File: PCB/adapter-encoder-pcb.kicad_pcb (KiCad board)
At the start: 4 copper layers, 14 x 15.6 mm, 33 parts, among them IC1 THVD2410VDRCR, M1 THRU_HOLE_PAD, M2 THRU_HOLE_PAD, U1 TLE5009E1000FUMA1, U2 STM32G031G6U6, U3 DF52-4S-0.8H(21), U4 SPX3819M5-L-3-3, U5 C2901617, U6 DF52-4S-0.8H(21), U7 SPX3819M5-L-3-3

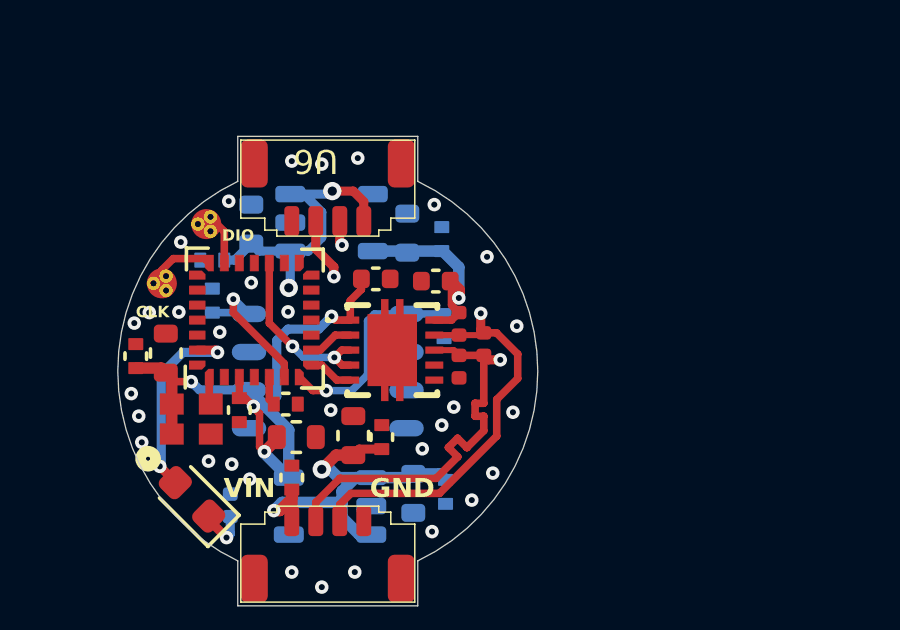
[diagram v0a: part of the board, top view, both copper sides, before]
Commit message: removed bad biasing resistors
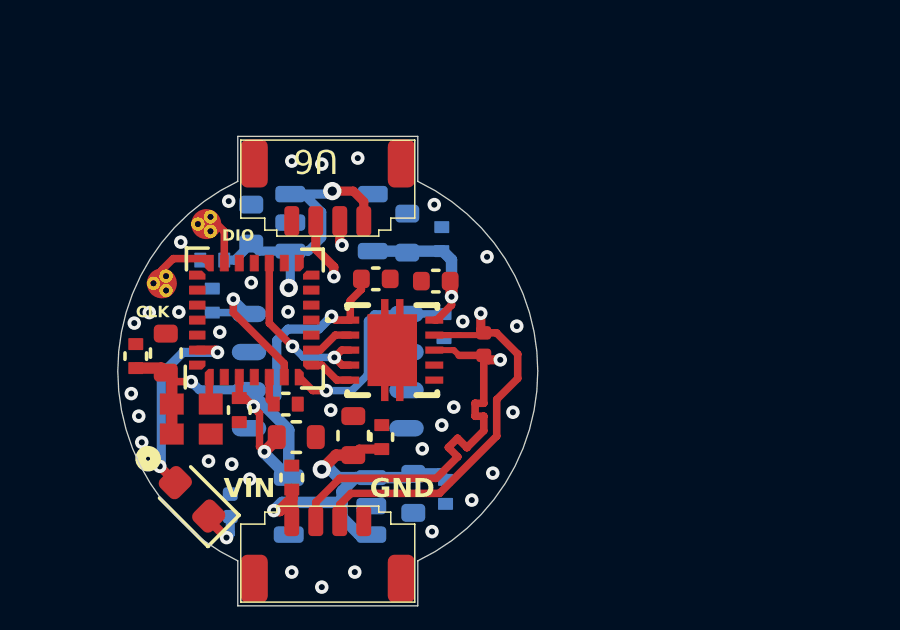
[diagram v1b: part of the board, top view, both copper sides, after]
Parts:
- removed R2, R4: 1k, adapter-encoder:R_0402_1005Metric
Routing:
- net /+5V0: track 6.90 -> 6.05 mm
- net GND: vias 31 -> 32
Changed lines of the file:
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@@
       (net 19 "/SWDIO") (pinfunction "1") (pintype "passive") (solder_mask_margin 0.0508))
-  )
-  (footprint "adapter-encoder:R_0402_1005Metric" (layer "F.Cu")
-    (at 149.279448 111.487448 90)
-    (descr "Resistor SMD 0402 (1005 Metric), square (rectangular) end terminal, IPC_7351 nominal, (Body size source: IPC-SM-782 page 72, https://www.pcb-3d.com/wordpress/wp-content/uploads/ipc-sm-782a_amendment_1_and_2.pdf), generated with kicad-footprint-generator")
-    (tags "resistor")
-    (property "Sheetfile" "adapter-encoder-pcb.kicad_sch")
-    (property "Sheetname" "")
-    (property "ki_description" "Resistor, US symbol")
-    (property "ki_keywords" "R res resistor")
-    (attr smd)
-    (fp_text reference "R4" (at 2.95 -1.45 90) (layer "F.SilkS") hide
-        (effects (font (size 1 1) (thickness 0.15)))
-    )
-    (fp_text value "1k" (at 0 1.17 90) (layer "F.Fab") hide
-        (effects (font (size 1 1) (thickness 0.15)))
-    )
-    (fp_text user "${REFERENCE}" (at 0 0 90) (layer "F.Fab")
-        (effects (font (size 0.26 0.26) (thickness 0.04)))
-    )
-    (fp_line (start -0.525 -0.27) (end 0.525 -0.27)
-      (stroke (width 0.1) (type solid)) (layer "F.Fab"))
-    (fp_line (start -0.525 0.27) (end -0.525 -0.27)
-      (stroke (width 0.1) (type solid)) (layer "F.Fab"))
-    (fp_line (start 0.525 -0.27) (end 0.525 0.27)
-      (stroke (width 0.1) (type solid)) (layer "F.Fab"))
-    (fp_line (start 0.525 0.27) (end -0.525 0.27)
-      (stroke (width 0.1) (type solid)) (layer "F.Fab"))
-    (pad "1" smd roundrect (at -0.375 0 90) (size 0.45 0.5) (layers "F.Cu" "F.Paste" "F.Mask") (roundrect_rratio 0.25)
-      (net 1 "GND") (pintype "passive") (solder_mask_margin 0.0508))
-    (pad "2" smd roundrect (at 0.375 0 90) (size 0.45 0.5) (layers "F.Cu" "F.Paste" "F.Mask") (roundrect_rratio 0.25)
-      (net 37 "/RS485+") (pintype "passive") (solder_mask_margin 0.0508))
-    (model "${KICAD6_3DMODEL_DIR}/Resistor_SMD.3dshapes/R_0402_1005Metric.wrl"
-      (offset (xyz 0 0 0))
-      (scale (xyz 1 1 1))
-      (rotate (xyz 0 0 0))
-    )
   )
   (footprint "adapter-encoder:C_0402_1005Metric" (layer "F.Cu")
@@
   )
   (footprint "adapter-encoder:R_0402_1005Metric" (layer "F.Cu")
-    (at 149.279448 110.062448 90)
-    (descr "Resistor SMD 0402 (1005 Metric), square (rectangular) end terminal, IPC_7351 nominal, (Body size source: IPC-SM-782 page 72, https://www.pcb-3d.com/wordpress/wp-content/uploads/ipc-sm-782a_amendment_1_and_2.pdf), generated with kicad-footprint-generator")
-    (tags "resistor")
-    (property "Sheetfile" "adapter-encoder-pcb.kicad_sch")
-    (property "Sheetname" "")
-    (property "ki_description" "Resistor, US symbol")
-    (property "ki_keywords" "R res resistor")
-    (attr smd)
-    (fp_text reference "R2" (at 2.95 -1.45 90) (layer "F.SilkS") hide
-        (effects (font (size 1 1) (thickness 0.15)))
-    )
-    (fp_text value "1k" (at 0 1.17 90) (layer "F.Fab") hide
-        (effects (font (size 1 1) (thickness 0.15)))
-    )
-    (fp_text user "${REFERENCE}" (at 0 0 90) (layer "F.Fab")
-        (effects (font (size 0.26 0.26) (thickness 0.04)))
-    )
-    (fp_line (start -0.525 -0.27) (end 0.525 -0.27)
-      (stroke (width 0.1) (type solid)) (layer "F.Fab"))
-    (fp_line (start -0.525 0.27) (end -0.525 -0.27)
-      (stroke (width 0.1) (type solid)) (layer "F.Fab"))
-    (fp_line (start 0.525 -0.27) (end 0.525 0.27)
-      (stroke (width 0.1) (type solid)) (layer "F.Fab"))
-    (fp_line (start 0.525 0.27) (end -0.525 0.27)
-      (stroke (width 0.1) (type solid)) (layer "F.Fab"))
-    (pad "1" smd roundrect (at -0.375 0 90) (size 0.45 0.5) (layers "F.Cu" "F.Paste" "F.Mask") (roundrect_rratio 0.25)
-      (net 38 "/RS485-") (pintype "passive") (solder_mask_margin 0.0508))
-    (pad "2" smd roundrect (at 0.375 0 90) (size 0.45 0.5) (layers "F.Cu" "F.Paste" "F.Mask") (roundrect_rratio 0.25)
-      (net 21 "/+5V0") (pintype "passive") (solder_mask_margin 0.0508))
-    (model "${KICAD6_3DMODEL_DIR}/Resistor_SMD.3dshapes/R_0402_1005Metric.wrl"
-      (offset (xyz 0 0 0))
-      (scale (xyz 1 1 1))
-      (rotate (xyz 0 0 0))
-    )
-  )
-  (footprint "adapter-encoder:R_0402_1005Metric" (layer "F.Cu")
     (at 150.104448 110.737448 90)
     (descr "Resistor SMD 0402 (1005 Metric), square (rectangular) end terminal, IPC_7351 nominal, (Body size source: IPC-SM-782 page 72, https://www.pcb-3d.com/wordpress/wp-content/uploads/ipc-sm-782a_amendment_1_and_2.pdf), generated with kicad-footprint-generator")
@@
   (via (at 148.054048 114.228248) (size 0.45) (drill 0.2) (layers "F.Cu" "B.Cu") (net 1))
   (via (at 145.004448 112.937448) (size 0.45) (drill 0.2) (layers "F.Cu" "B.Cu") (net 1))
+  (via (at 149.404448 109.983848) (size 0.45) (drill 0.2) (layers "F.Cu" "B.Cu") (net 1))
   (via (at 143.704448 118.337448) (size 0.45) (drill 0.2) (layers "F.Cu" "B.Cu") (net 1))
   (via (at 138.704448 114.012448) (size 0.45) (drill 0.2) (layers "F.Cu" "B.Cu") (net 1))
@@
   (segment (start 141.454448 106.982281) (end 140.984448 106.512281) (width 0.254) (layer "F.Cu") (net 20))
   (segment (start 141.454448 108.037448) (end 141.454448 106.982281) (width 0.254) (layer "F.Cu") (net 20))
-  (segment (start 149.273248 108.926248) (end 148.984448 108.637448) (width 0.4) (layer "F.Cu") (net 21))
-  (segment (start 149.029448 109.937448) (end 149.279448 109.687448) (width 0.254) (layer "F.Cu") (net 21))
   (segment (start 149.029448 108.682448) (end 149.029448 109.437448) (width 0.254) (layer "F.Cu") (net 21))
-  (segment (start 149.273248 109.199048) (end 149.273248 108.926248) (width 0.4) (layer "F.Cu") (net 21))
-  (segment (start 148.454448 109.937448) (end 149.029448 109.937448) (width 0.254) (layer "F.Cu") (net 21))
+  (segment (start 149.029448 109.157448) (end 149.029448 108.682448) (width 0.4) (layer "F.Cu") (net 21))
   (segment (start 148.984448 108.637448) (end 149.029448 108.682448) (width 0.254) (layer "F.Cu") (net 21))
-  (segment (start 149.029448 109.437448) (end 149.279448 109.687448) (width 0.254) (layer "F.Cu") (net 21))
-  (via (at 149.273248 109.199048) (size 0.45) (drill 0.2) (layers "F.Cu" "B.Cu") (net 21))
+  (segment (start 148.454448 109.937448) (end 148.529448 109.937448) (width 0.254) (layer "F.Cu") (net 21))
+  (segment (start 148.529448 109.937448) (end 149.029448 109.437448) (width 0.254) (layer "F.Cu") (net 21))
+  (via (at 149.029448 109.157448) (size 0.45) (drill 0.2) (layers "F.Cu" "B.Cu") (net 21))
+  (segment (start 149.029448 109.157448) (end 149.029448 107.927386) (width 0.381) (layer "B.Cu") (net 21))
+  (segment (start 149.029448 107.927386) (end 148.73951 107.637448) (width 0.381) (layer "B.Cu") (net 21))
+  (segment (start 148.704448 107.637448) (end 146.404448 107.637448) (width 0.381) (layer "B.Cu") (net 21))
   (segment (start 148.73951 107.637448) (end 148.704448 107.637448) (width 0.381) (layer "B.Cu") (net 21))
-  (segment (start 149.273248 108.171186) (end 148.73951 107.637448) (width 0.381) (layer "B.Cu") (net 21))
-  (segment (start 149.273248 109.199048) (end 149.273248 108.171186) (width 0.381) (layer "B.Cu") (net 21))
-  (segment (start 148.704448 107.637448) (end 146.404448 107.637448) (width 0.381) (layer "B.Cu") (net 21))
   (segment (start 145.654448 110.937448) (end 145.367581 110.937448) (width 0.25) (layer "F.Cu") (net 22))
   (segment (start 143.727448 110.81185) (end 142.954448 110.03885) (width 0.25) (layer "F.Cu") (net 22))
